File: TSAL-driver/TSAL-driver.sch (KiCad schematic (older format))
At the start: 11 parts, among them J1 LED+, J2 LED-, J3 12V, J4 GND, U1 AZ1117-5.0, U2 ATtiny25-20SSU, U3 LDB-350L

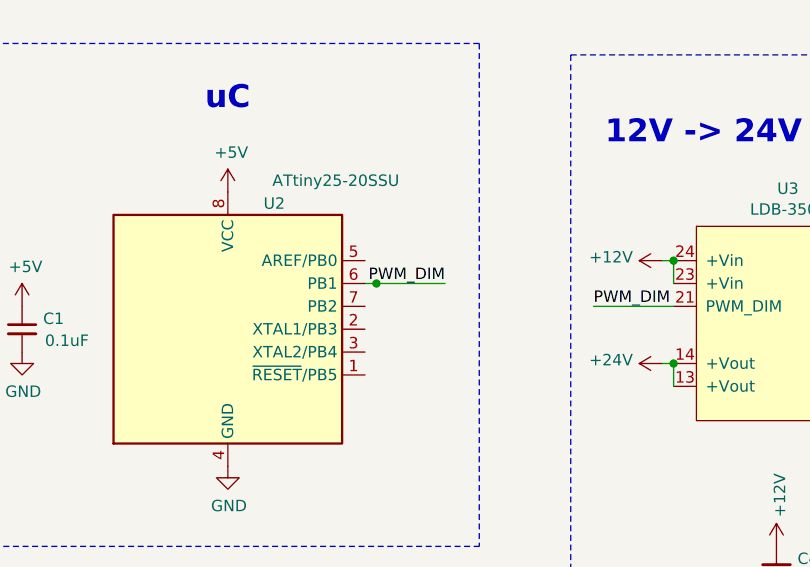
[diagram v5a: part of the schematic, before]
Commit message: New LDB footprint
Completed TSAL
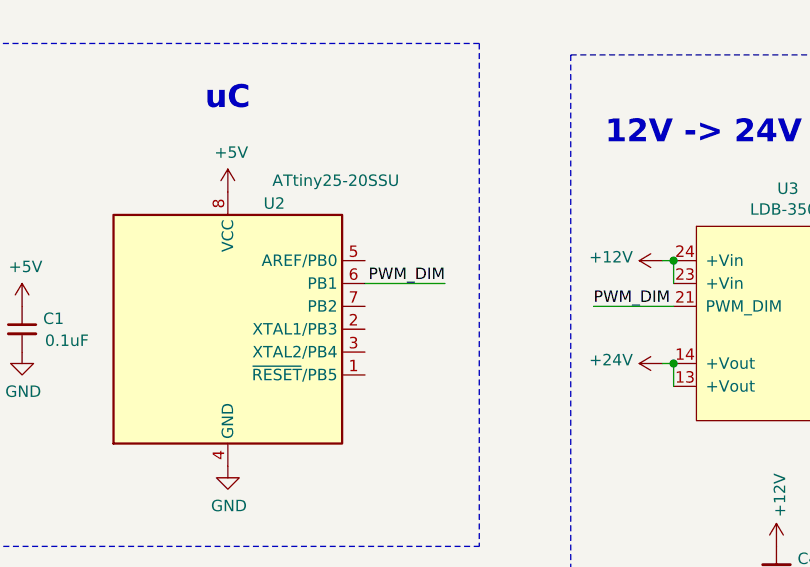
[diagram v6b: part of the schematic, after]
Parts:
- U3: footprint AERO-footprints:DIP1549W45P254L3404H940Q24 -> AERO-footprints:LDB-_L
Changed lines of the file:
@@
 F 0 "U3" H 6100 3765 50  0000 C CNN
 F 1 "LDB-350L" H 6100 3674 50  0000 C CNN
-F 2 "AERO-footprints:DIP1549W45P254L3404H940Q24" H 6250 3200 50  0001 C CNN
+F 2 "AERO-footprints:LDB-_L" H 6250 3200 50  0001 C CNN
 F 3 "" H 6250 3200 50  0001 C CNN
 	1    6100 3150
@@
 	-1   0    0    1
 $EndComp
-Wire Wire Line
-	4600 2950 4300 2950
 Text Label 4600 2950 2    50   ~ 0
 PWM_DIM
@@
 	1    0    0    -1
 $EndComp
-Connection ~ 4300 2950
-Wire Wire Line
-	4300 2950 4250 2950
 $Comp
 L Device:C_Small C1
@@
 	1    0    0    -1
 $EndComp
+Wire Wire Line
+	4250 2950 4600 2950
 $EndSCHEMATC
